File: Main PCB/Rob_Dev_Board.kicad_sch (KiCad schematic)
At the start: 9 parts, among them J1 TYPE-C-31-M-12, U1 DRV8245HQRXZRQ1, U2 ESP32-S3-WROOM-1U-N16R8, U3 DRV8245HQRXZRQ1, U4 PCA9685PW_118

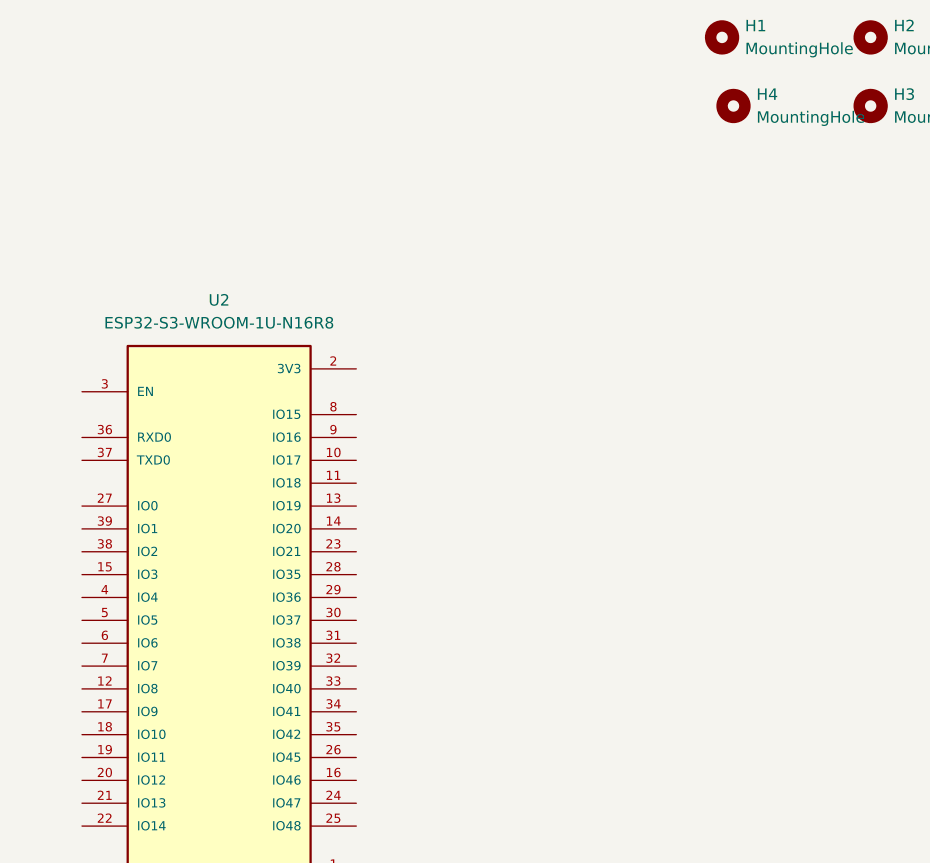
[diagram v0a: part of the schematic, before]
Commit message: Added acceler. and connector type to part library
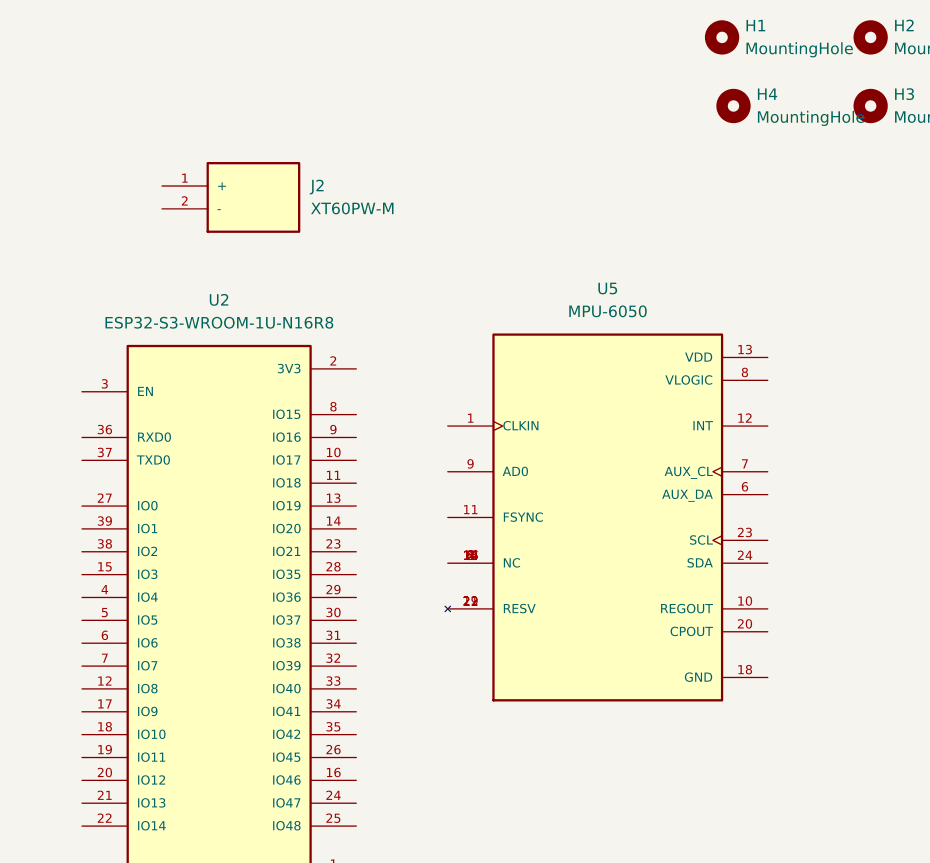
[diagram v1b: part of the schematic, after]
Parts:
- added J2: XT60PW-M, XT60PW-M Connector:AMASS_XT60PW-M, symbol XT60PW-M Connector:XT60PW-M
- added U5: MPU-6050, MPU-6050 Accelerometer:QFN50P400X400X95-24N, symbol MPU-6050 Accelerometer:MPU-6050
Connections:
- new net: U5.14 (NC), U5.15 (NC), U5.16 (NC), U5.17 (NC), U5.2 (NC), U5.3 (NC), U5.4 (NC), U5.5 (NC)
- new net: U5.19 (RESV), U5.21 (RESV), U5.22 (RESV)

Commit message: Testing
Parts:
- added J10, J11, J12, J3, J4, J5, J6, J7, J8, J9: XT60PW-M, XT60PW-M Connector:AMASS_XT60PW-M, symbol XT60PW-M Connector:XT60PW-M
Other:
- moved on the sheet: H1, H2, H3, H4, J1, J2, U2, U5
